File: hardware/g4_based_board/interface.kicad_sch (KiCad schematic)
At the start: 13 parts, among them J1 USB_C_Receptacle_USB2.0, J2 Micro_SD_Card_Det1, Q1 NPN, Q2 NPN

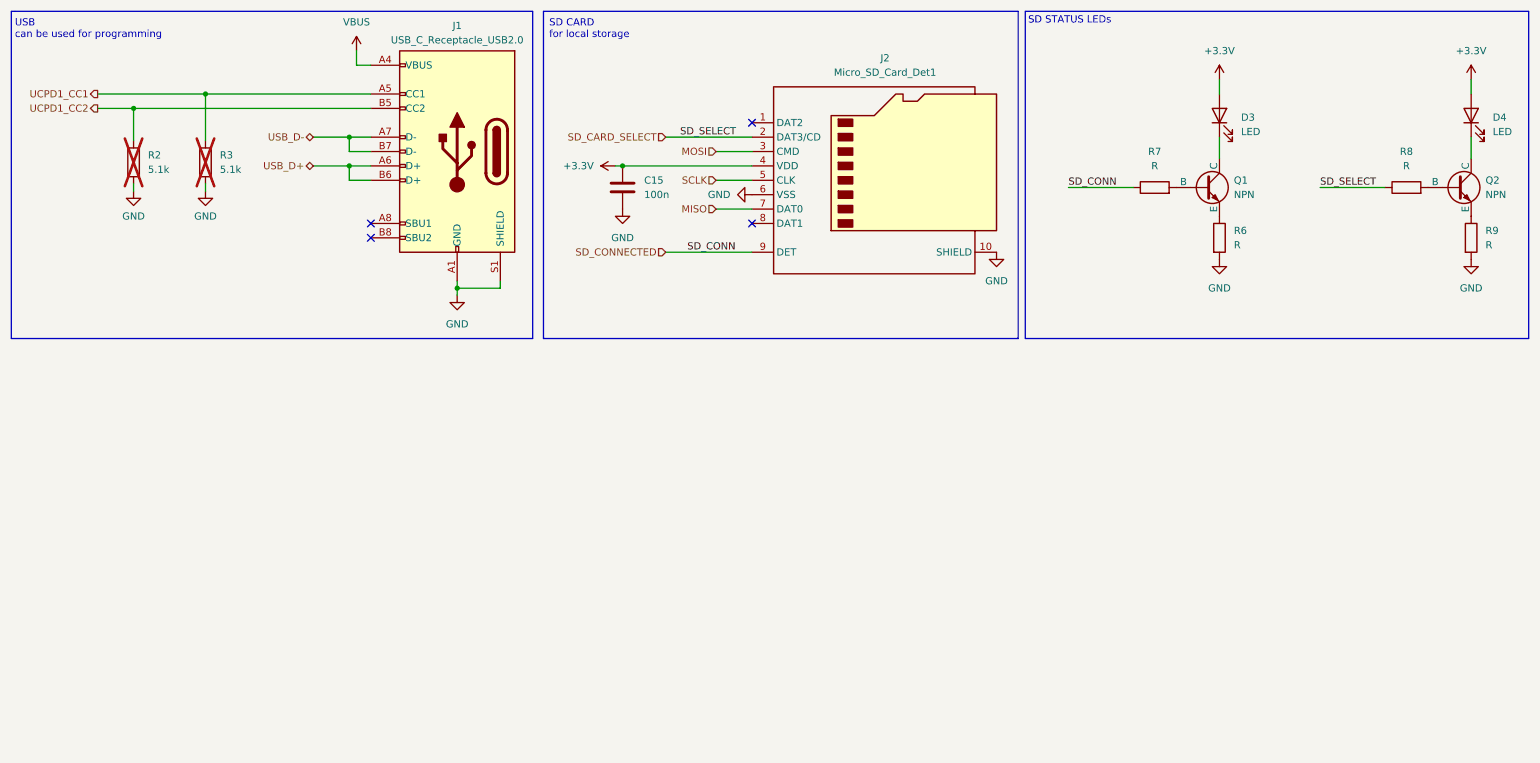
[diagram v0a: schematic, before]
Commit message: added tvs proctection didoes
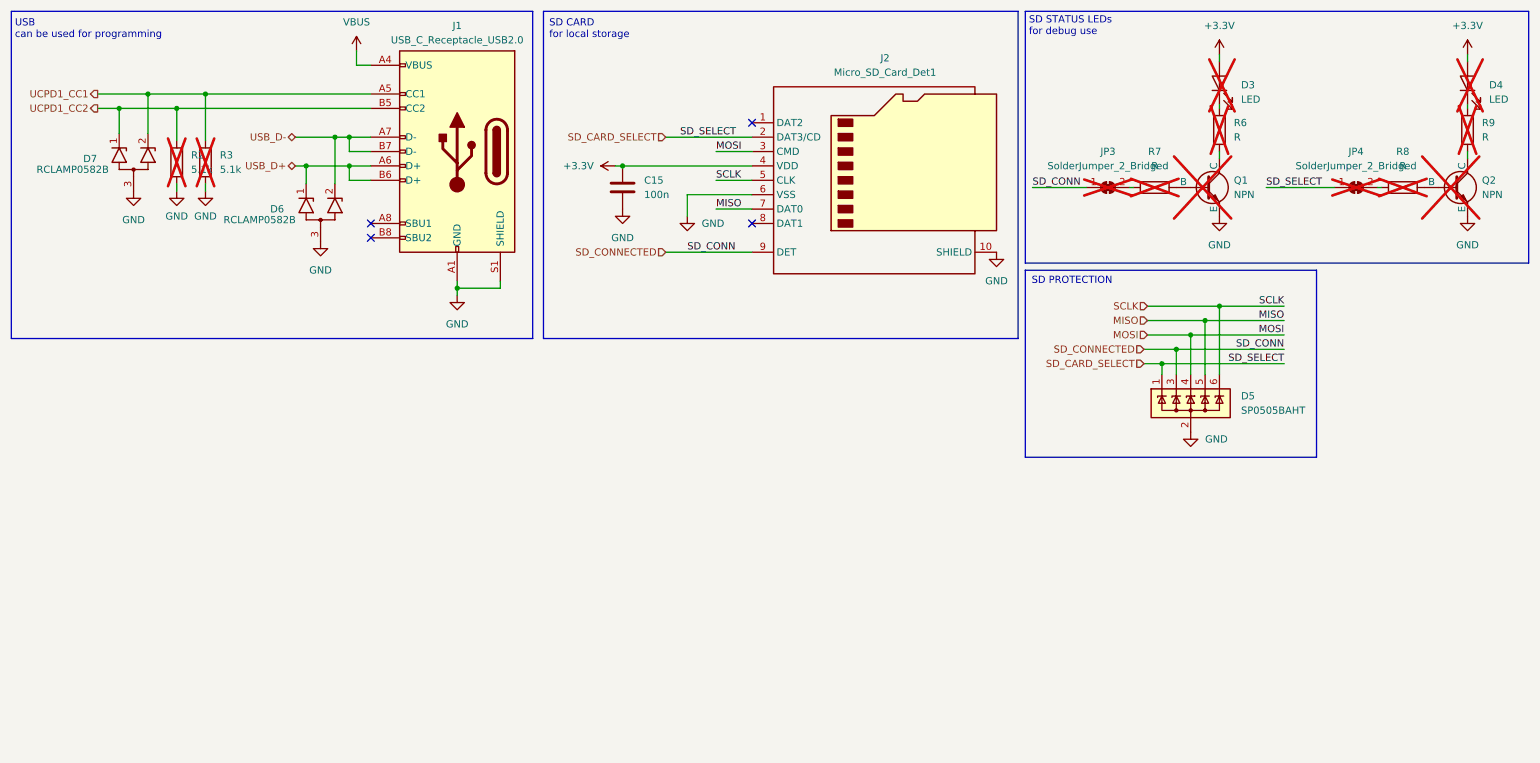
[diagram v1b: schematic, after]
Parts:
- added D5: SP0505BAHT, Package_TO_SOT_SMD:SOT-23-6, symbol Power_Protection:SP0505BAHT
- added D6, D7: RCLAMP0582B, Package_TO_SOT_SMD:SOT-416, symbol Power_Protection:RCLAMP0582B
- added JP3, JP4: SolderJumper_2_Bridged, symbol Jumper:SolderJumper_2_Bridged
- D3, D4, Q1, Q2, R6, R7, R8, R9: now not fitted
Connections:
- net GND: now also Q1.3 (E), Q2.3 (E), D5.2 (A), D6.3 (A), D7.3 (A); no longer R6.2, R9.2
- net MISO: now also D5.5 (K)
- net MOSI: now also D5.4 (K)
- net SCLK: now also D5.6 (K)
- net SD_CARD_SELECT: now also D5.1 (K), JP4.1 (A); no longer R8.1
- net SD_CONNECTED: now also D5.3 (K), JP3.1 (A); no longer R7.1
- net UCPD1_CC1: now also D7.2 (K2)
- net UCPD1_CC2: now also D7.1 (K1)
- net USB_D+: now also D6.1 (K1)
- net USB_D-: now also D6.2 (K2)
- net at Q2.1 (C): now also R9.2; no longer D4.1 (K)
- net at R9.1: now also D4.1 (K); no longer Q2.3 (E)
- net at D3.1 (K): now also R6.1; no longer Q1.1 (C)
- new net: JP3.2 (B), R7.1
- new net: Q1.1 (C), R6.2
- new net: JP4.2 (B), R8.1
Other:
- note added: "SD PROTECTION"
- note added: "SD STATUS LEDs for debug use"
- note removed: "SD STATUS LEDs"
- moved on the sheet: R2

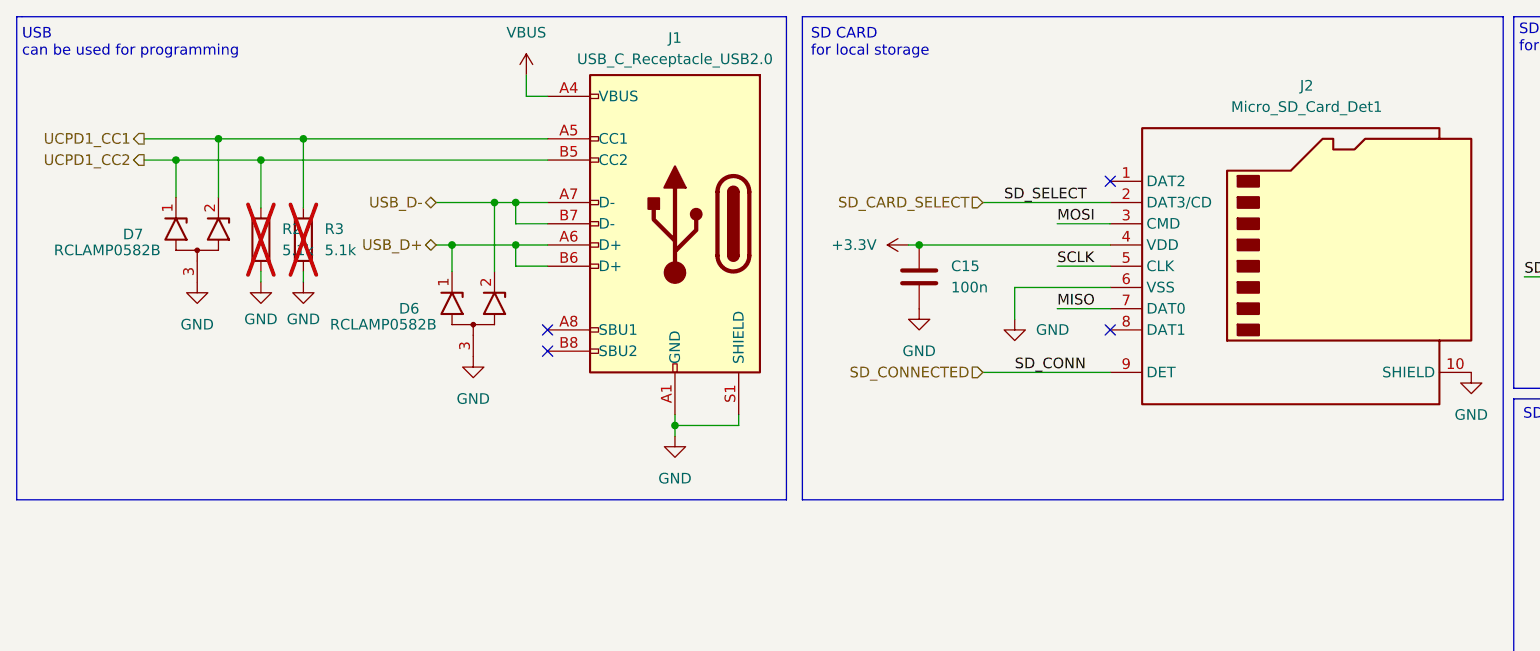
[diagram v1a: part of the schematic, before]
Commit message: removed half of the digial interfaces and added the thermocouples and LCD modules in to this sheet
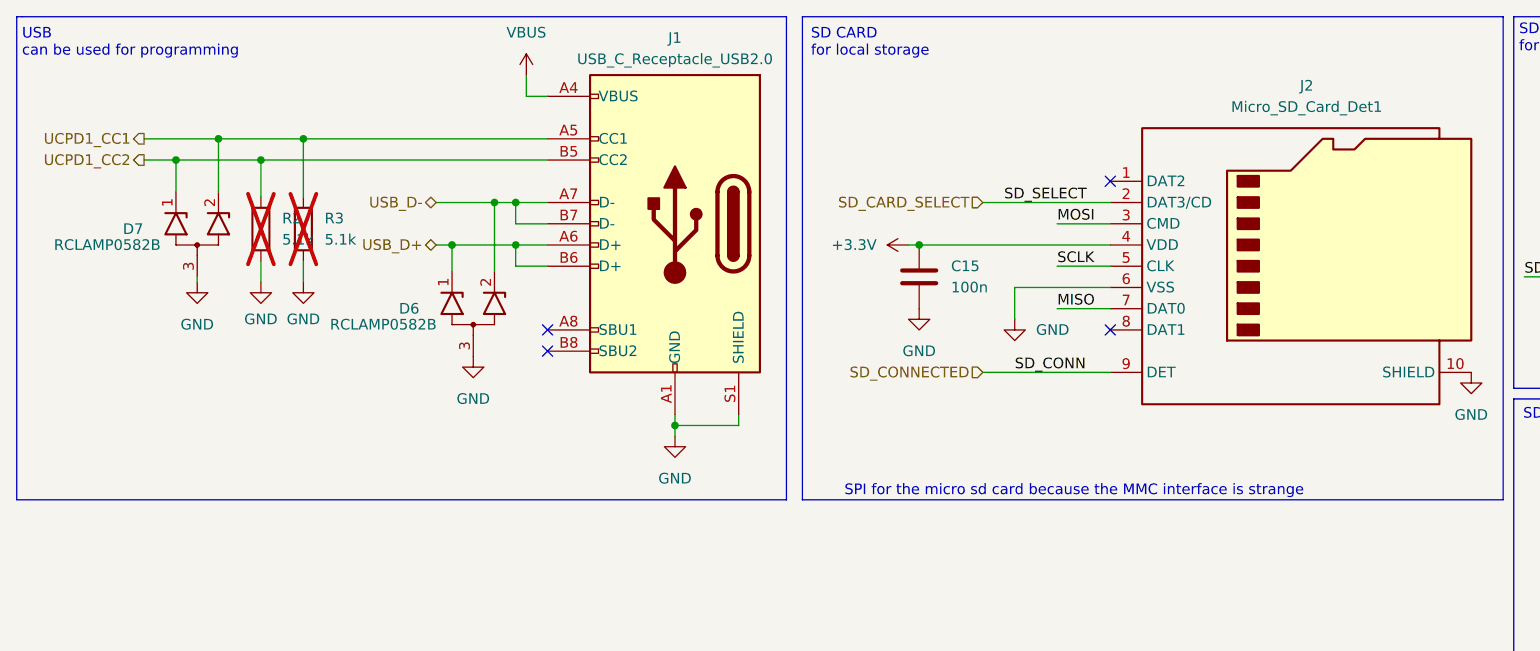
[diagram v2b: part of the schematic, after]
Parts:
- R2, R3: footprint Resistor_SMD:R_0805_2012Metric_Pad1.20x1.40mm_HandSolder -> Resistor_SMD:R_0805_2012Metric
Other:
- note added: "SPI for the micro sd card because the MMC interface is strange"
- moved on the sheet: D7, R2, R3
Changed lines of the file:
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@@
 	(wire
 		(pts
-			(xy 34.29 31.75) (xy 34.29 36.195)
+			(xy 34.29 31.75) (xy 34.29 35.56)
 		)
 		(stroke
@@
 	(wire
 		(pts
+			(xy 36.83 45.72) (xy 36.83 46.355)
+		)
+		(stroke
+			(width 0)
+			(type default)
+		)
+	)
+	(wire
+		(pts
 			(xy 65.405 36.83) (xy 72.39 36.83)
 		)
@@
 	(wire
 		(pts
-			(xy 49.53 45.085) (xy 49.53 46.355)
+			(xy 49.53 43.815) (xy 49.53 46.355)
 		)
 		(stroke
@@
 	(wire
 		(pts
-			(xy 44.45 45.085) (xy 44.45 46.355)
+			(xy 44.45 43.815) (xy 44.45 46.355)
 		)
 		(stroke
@@
 	(wire
 		(pts
-			(xy 49.53 29.21) (xy 49.53 37.465)
+			(xy 49.53 29.21) (xy 49.53 36.195)
 		)
 		(stroke
@@
 	(wire
 		(pts
-			(xy 44.45 31.75) (xy 44.45 37.465)
+			(xy 44.45 31.75) (xy 44.45 36.195)
 		)
 		(stroke
@@
 	(wire
 		(pts
-			(xy 39.37 29.21) (xy 39.37 36.195)
+			(xy 39.37 29.21) (xy 39.37 35.56)
 		)
 		(stroke
@@
 		)
 	)
+	(text "SPI for the micro sd card because the MMC interface is strange\n"
+		(exclude_from_sim no)
+		(at 141.732 71.374 0)
+		(effects
+			(font
+				(size 1.27 1.27)
+			)
+		)
+	)
 	(label "MISO"
 		(at 139.7 49.53 0)
@@
 	(symbol
 		(lib_id "Device:R")
-		(at 44.45 41.275 0)
+		(at 44.45 40.005 0)
 		(unit 1)
 		(exclude_from_sim no)
@@
 		(fields_autoplaced yes)
 		(property "Reference" "R2"
-			(at 46.99 40.005 0)
+			(at 46.99 38.735 0)
 			(effects
 				(font
@@
 		)
 		(property "Value" "5.1k"
-			(at 46.99 42.545 0)
+			(at 46.99 41.275 0)
 			(effects
 				(font
@@
 			)
 		)
-		(property "Footprint" "Resistor_SMD:R_0805_2012Metric_Pad1.20x1.40mm_HandSolder"
-			(at 42.672 41.275 90)
+		(property "Footprint" "Resistor_SMD:R_0805_2012Metric"
+			(at 42.672 40.005 90)
 			(effects
 				(font
@@
 		)
 		(property "Datasheet" "~"
-			(at 44.45 41.275 0)
+			(at 44.45 40.005 0)
 			(effects
 				(font
@@
 		)
 		(property "Description" ""
-			(at 44.45 41.275 0)
+			(at 44.45 40.005 0)
 			(effects
 				(font
@@
 	(symbol
 		(lib_id "Device:R")
-		(at 49.53 41.275 0)
+		(at 49.53 40.005 0)
 		(unit 1)
 		(exclude_from_sim no)
@@
 		(fields_autoplaced yes)
 		(property "Reference" "R3"
-			(at 52.07 40.005 0)
+			(at 52.07 38.735 0)
 			(effects
 				(font
@@
 		)
 		(property "Value" "5.1k"
-			(at 52.07 42.545 0)
+			(at 52.07 41.275 0)
 			(effects
 				(font
@@
 			)
 		)
-		(property "Footprint" "Resistor_SMD:R_0805_2012Metric_Pad1.20x1.40mm_HandSolder"
-			(at 47.752 41.275 90)
+		(property "Footprint" "Resistor_SMD:R_0805_2012Metric"
+			(at 47.752 40.005 90)
 			(effects
 				(font
@@
 		)
 		(property "Datasheet" "~"
-			(at 49.53 41.275 0)
+			(at 49.53 40.005 0)
 			(effects
 				(font
@@
 		)
 		(property "Description" ""
-			(at 49.53 41.275 0)
+			(at 49.53 40.005 0)
 			(effects
 				(font
@@
 	(symbol
 		(lib_id "Power_Protection:RCLAMP0582B")
-		(at 36.83 41.275 90)
+		(at 36.83 40.64 90)
 		(unit 1)
 		(exclude_from_sim no)
@@
 		(dnp no)
 		(property "Reference" "D7"
-			(at 27.94 40.64 90)
+			(at 27.94 40.005 90)
 			(effects
 				(font
@@
 		)
 		(property "Value" "RCLAMP0582B"
-			(at 19.685 42.545 90)
+			(at 19.685 41.91 90)
 			(effects
 				(font
@@
 		)
 		(property "Footprint" "Package_TO_SOT_SMD:SOT-416"
-			(at 44.45 41.275 0)
+			(at 44.45 40.64 0)
 			(effects
 				(font
@@
 		)
 		(property "Datasheet" "https://www.semtech.com/products/circuit-protection/low-capacitance/rclamp0582b"
-			(at 34.29 40.005 0)
+			(at 34.29 39.37 0)
 			(effects
 				(font
@@
 		)
 		(property "Description" "Low capacitance unidirectional dual ESD protection diode, SC-75"
-			(at 36.83 41.275 0)
+			(at 36.83 40.64 0)
 			(effects
 				(font

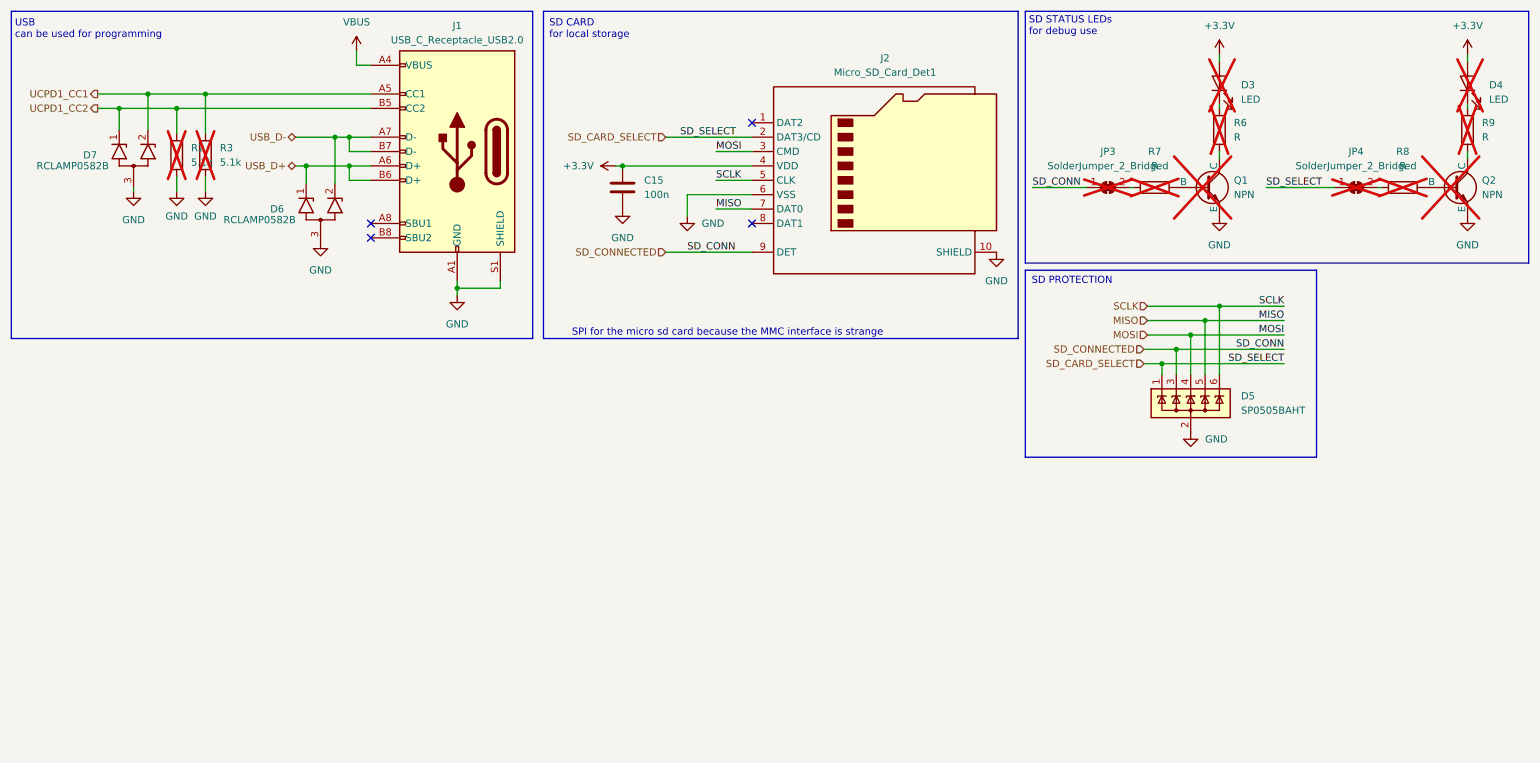
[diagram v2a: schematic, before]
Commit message: added jumpers to the micro SD card as well as a schotty to the VBus of the type c for safety
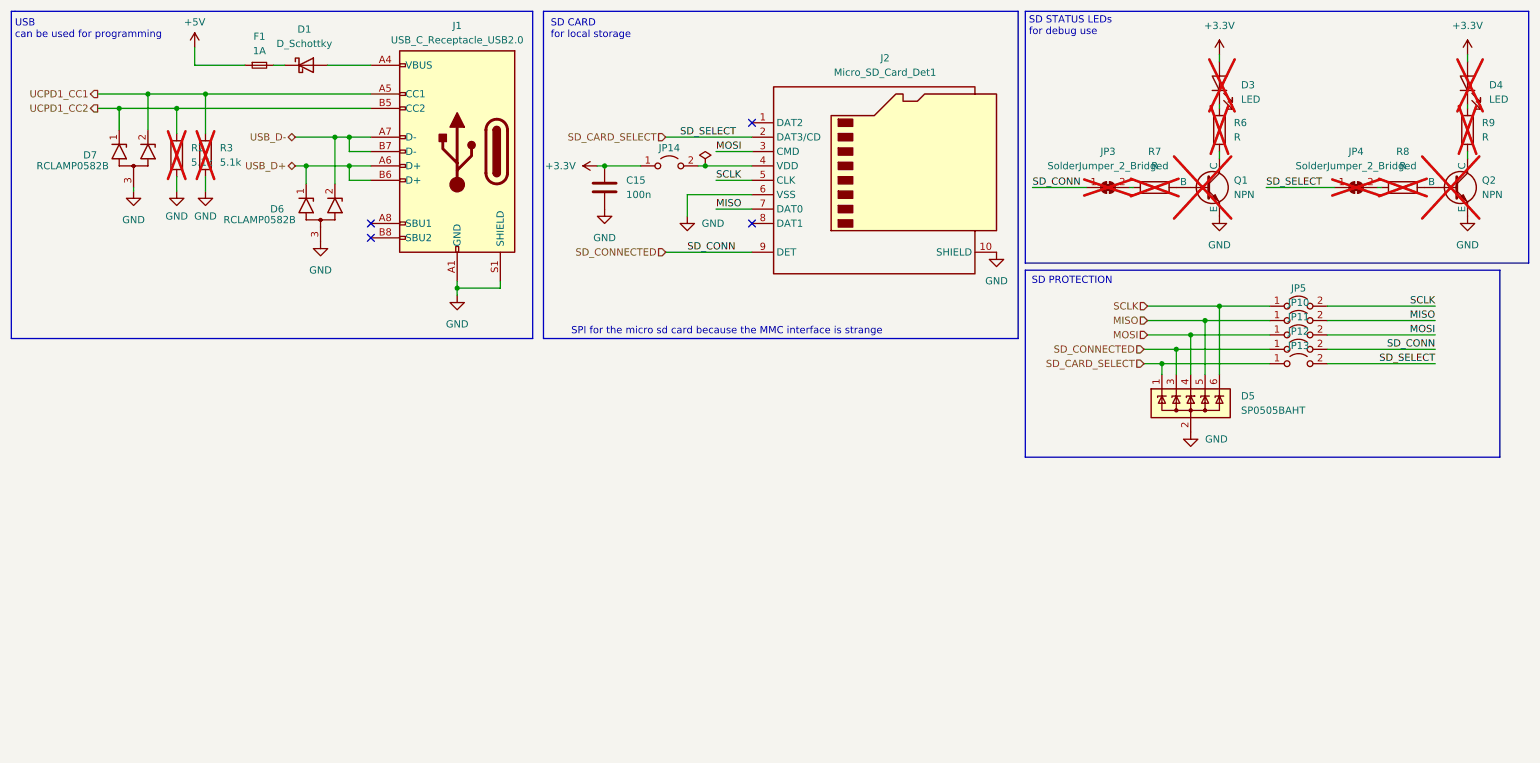
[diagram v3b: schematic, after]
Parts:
- added D1: D_Schottky, Diode_SMD:D_0805_2012Metric_Pad1.15x1.40mm_HandSolder, symbol Device:D_Schottky
- added F1: 1A, Fuse:Fuse_0805_2012Metric_Pad1.15x1.40mm_HandSolder, symbol Device:Fuse_Small
- added JP10, JP11, JP12, JP13, JP14, JP5: Jumper_2_Open, Jumper:SolderJumper-2_P1.3mm_Open_TrianglePad1.0x1.5mm, symbol Jumper:Jumper_2_Open
- C15: footprint Capacitor_SMD:C_0805_2012Metric -> Capacitor_SMD:C_0603_1608Metric_Pad1.08x0.95mm_HandSolder
- JP3, JP4: footprint (none) -> Jumper:SolderJumper-2_P1.3mm_Bridged_Pad1.0x1.5mm
- R2, R3, R6, R7, R8, R9: footprint Resistor_SMD:R_0805_2012Metric -> Resistor_SMD:R_0603_1608Metric_Pad0.98x0.95mm_HandSolder
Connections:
- net +3.3V: now also JP14.1 (A); no longer J2.4 (VDD)
- net MISO: now also JP10.1 (A), JP10.2 (B)
- net MOSI: now also JP11.1 (A), JP11.2 (B)
- net SCLK: now also JP5.1 (A), JP5.2 (B)
- net SD_CARD_SELECT: now also JP13.1 (A), JP13.2 (B)
- net SD_CONNECTED: now also JP12.1 (A), JP12.2 (B)
- net VBUS: no longer names the net of J1.A4 (VBUS), J1.A9 (VBUS), J1.B4 (VBUS), J1.B9 (VBUS)
- net VBUS: now also D1.2 (A)
- new net: J2.4 (VDD), JP14.2 (B)
- new net: D1.1 (K), F1.2
- new net +5V: F1.1
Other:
- moved on the sheet: C15

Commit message: git thinks something changed in this file
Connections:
- net at J1.A4 (VBUS), J1.A9 (VBUS), J1.B4 (VBUS)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: now also D1.1 (K); no longer D1.2 (A)
- net at F1.2: now also D1.2 (A); no longer D1.1 (K)
- net +5V renamed VBUS

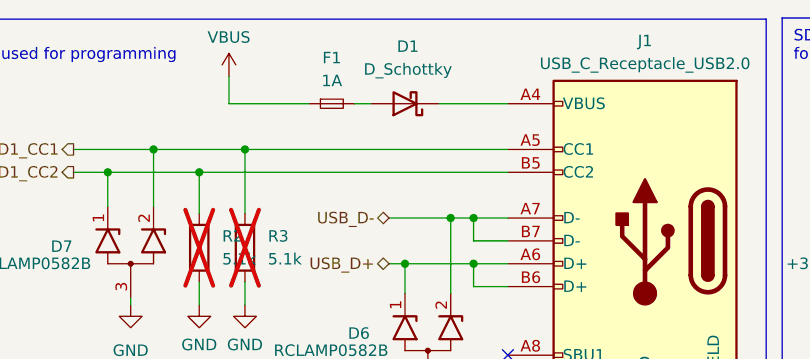
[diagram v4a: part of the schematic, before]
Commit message: changed 5v on the type c header to VBUS
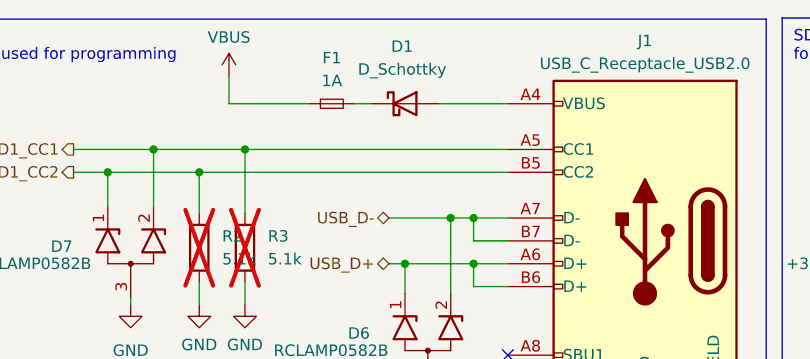
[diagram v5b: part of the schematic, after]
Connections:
- net at J1.A4 (VBUS), J1.A9 (VBUS), J1.B4 (VBUS)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: now also D1.2 (A); no longer D1.1 (K)
- net at F1.2: now also D1.1 (K); no longer D1.2 (A)
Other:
- moved on the sheet: D1
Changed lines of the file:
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@@
 	(symbol
 		(lib_id "Device:D_Schottky")
-		(at 67.31 24.13 180)
+		(at 67.31 24.13 0)
 		(unit 1)
 		(exclude_from_sim no)
@@
 		(fields_autoplaced yes)
 		(property "Reference" "D1"
-			(at 67.6275 17.78 0)
+			(at 66.9925 17.78 0)
 			(effects
 				(font
@@
 		)
 		(property "Value" "D_Schottky"
-			(at 67.6275 20.32 0)
+			(at 66.9925 20.32 0)
 			(effects
 				(font
